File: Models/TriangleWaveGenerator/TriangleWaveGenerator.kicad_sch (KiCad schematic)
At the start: 2 parts, among them U1 LF412CP, U2 LM311N/NOPB

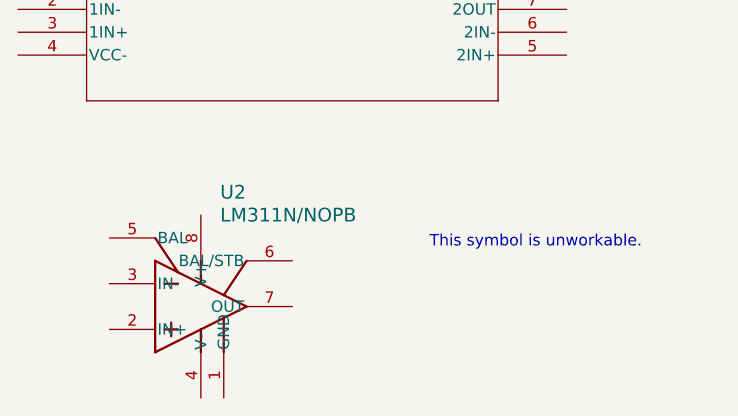
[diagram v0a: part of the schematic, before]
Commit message: Made custom symbol, much cleaner
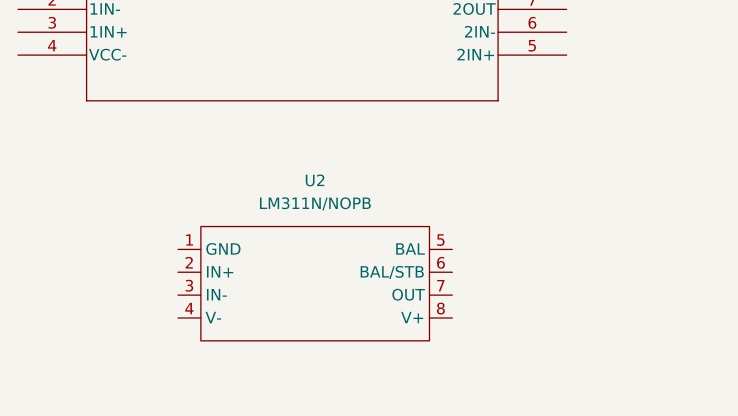
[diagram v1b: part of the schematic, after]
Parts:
- removed U2: LM311N/NOPB, N08E, symbol LM311:LM311N_NOPB
- added U2: LM311N/NOPB, symbol Custom:LM311N/NOPB
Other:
- note removed: "This symbol is unworkable."
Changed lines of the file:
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@@
 	(generator_version "9.0")
 	(paper "A4")
-	(text "This symbol is unworkable."
-		(exclude_from_sim no)
-		(at 139.7 108.966 0)
-		(effects
-			(font
-				(size 1.27 1.27)
-			)
-			(justify left top)
-		)
-	)
 	(symbol
-		(lib_id "LM311:LM311N_NOPB")
-		(at 109.22 111.76 0)
+		(lib_id "Custom:LM311N/NOPB")
+		(at 127 114.3 0)
 		(unit 1)
 		(exclude_from_sim no)
@@
 		(fields_autoplaced yes)
 		(property "Reference" "U2"
-			(at 116.4433 104.14 0)
+			(at 127 102.87 0)
 			(effects
 				(font
-					(size 1.524 1.524)
+					(size 1.27 1.27)
 				)
-				(justify left)
 			)
 		)
 		(property "Value" "LM311N/NOPB"
-			(at 116.4433 106.68 0)
-			(effects
-				(font
-					(size 1.524 1.524)
-				)
-				(justify left)
-			)
-		)
-		(property "Footprint" "N08E"
-			(at 109.22 111.76 0)
+			(at 127 105.41 0)
 			(effects
 				(font
 					(size 1.27 1.27)
-					(italic yes)
 				)
-				(hide yes)
 			)
 		)
-		(property "Datasheet" "https://www.ti.com/lit/gpn/lm311-n"
-			(at 109.22 111.76 0)
-			(effects
-				(font
-					(size 1.27 1.27)
-					(italic yes)
-				)
-				(hide yes)
-			)
-		)
-		(property "Description" ""
-			(at 109.22 111.76 0)
+		(property "Footprint" ""
+			(at 127 114.3 0)
 			(effects
 				(font
@@
 			)
 		)
+		(property "Datasheet" ""
+			(at 127 114.3 0)
+			(effects
+				(font
+					(size 1.27 1.27)
+				)
+				(hide yes)
+			)
+		)
+		(property "Description" ""
+			(at 127 114.3 0)
+			(effects
+				(font
+					(size 1.27 1.27)
+				)
+				(hide yes)
+			)
+		)
+		(pin "1"
+		)
 		(pin "2"
 		)
-		(pin "8"
+		(pin "3"
 		)
 		(pin "4"
 		)
-		(pin "1"
+		(pin "5"
 		)
 		(pin "6"
@@
 		(pin "7"
 		)
-		(pin "5"
-		)
-		(pin "3"
+		(pin "8"
 		)
 		(instances

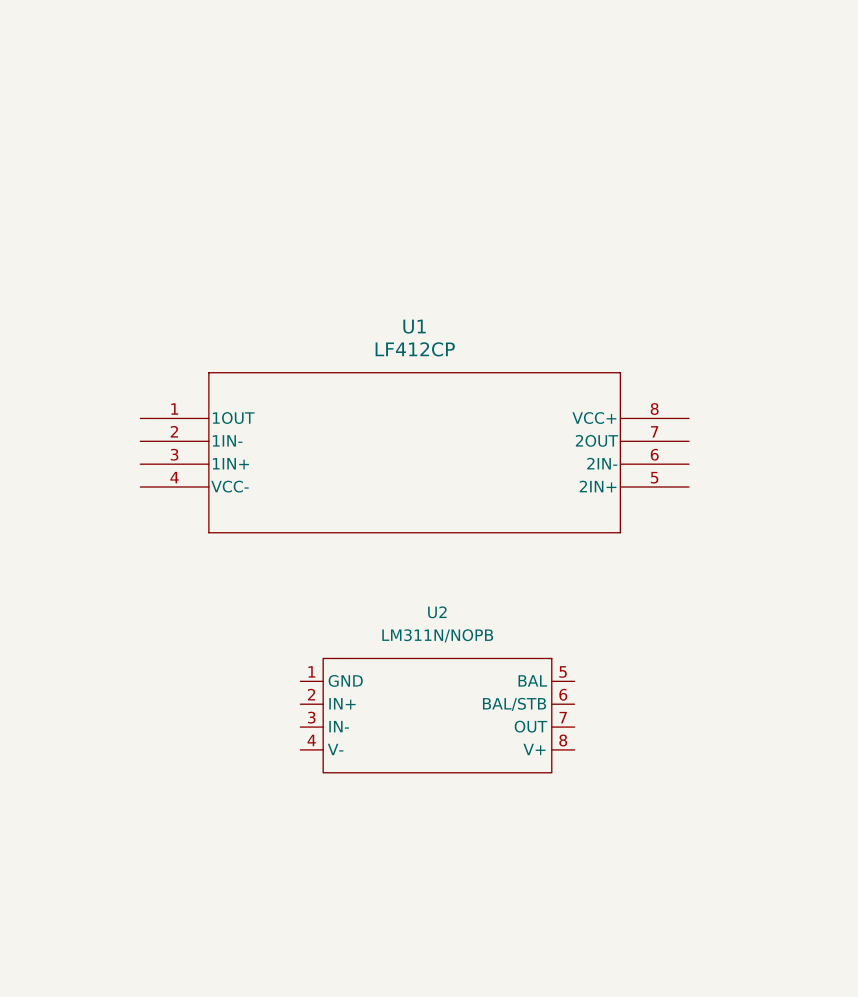
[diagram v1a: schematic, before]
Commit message: Need to migrate this to a hierarchical sheet
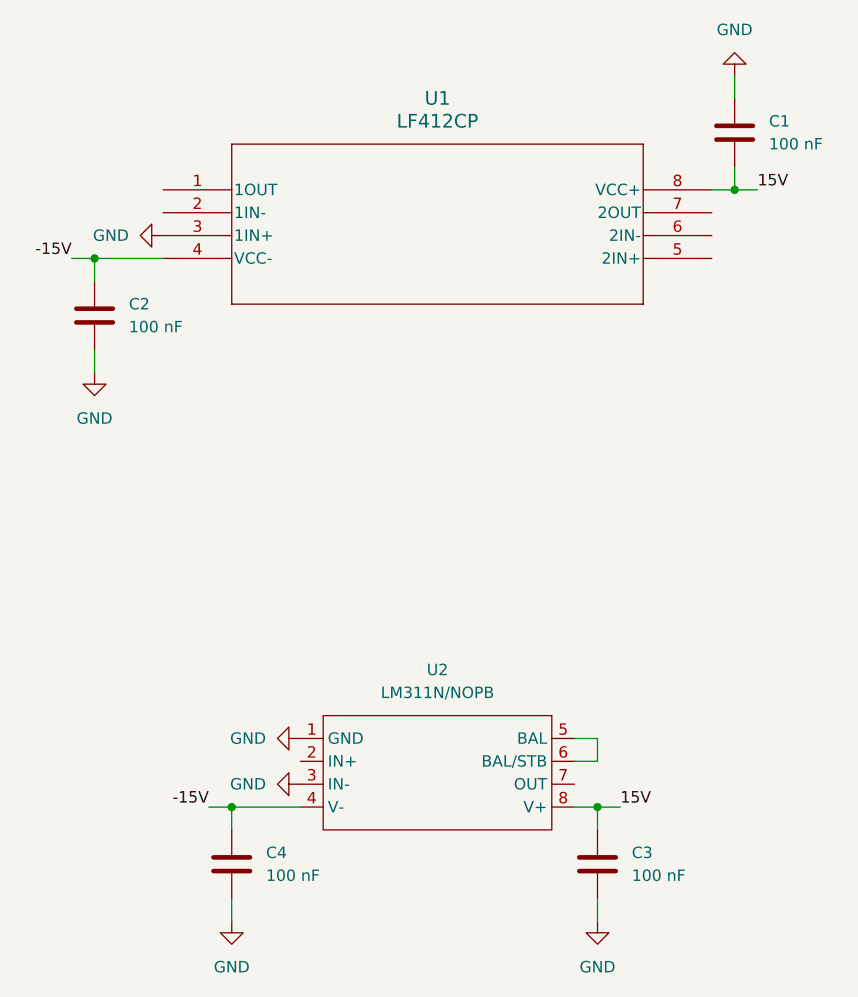
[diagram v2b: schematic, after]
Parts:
- added C1, C2, C3, C4: 100 nF, symbol Device:C
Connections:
- net GND: now reaches U2.1 (GND)
- net GND: now also U1.3 (1IN+), U2.3 (IN-), C1.1, C2.2, C3.2, C4.2
- net -15V: now reaches U2.4 (V-)
- net -15V: now also U1.4 (VCC-), C2.1, C4.1
- net at U2.5 (BAL): now also U2.6 (BAL/STB)
- net 15V: now reaches U2.8 (V+)
- net 15V: now also U1.8 (VCC+), C1.2, C3.1
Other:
- moved on the sheet: U1, U2

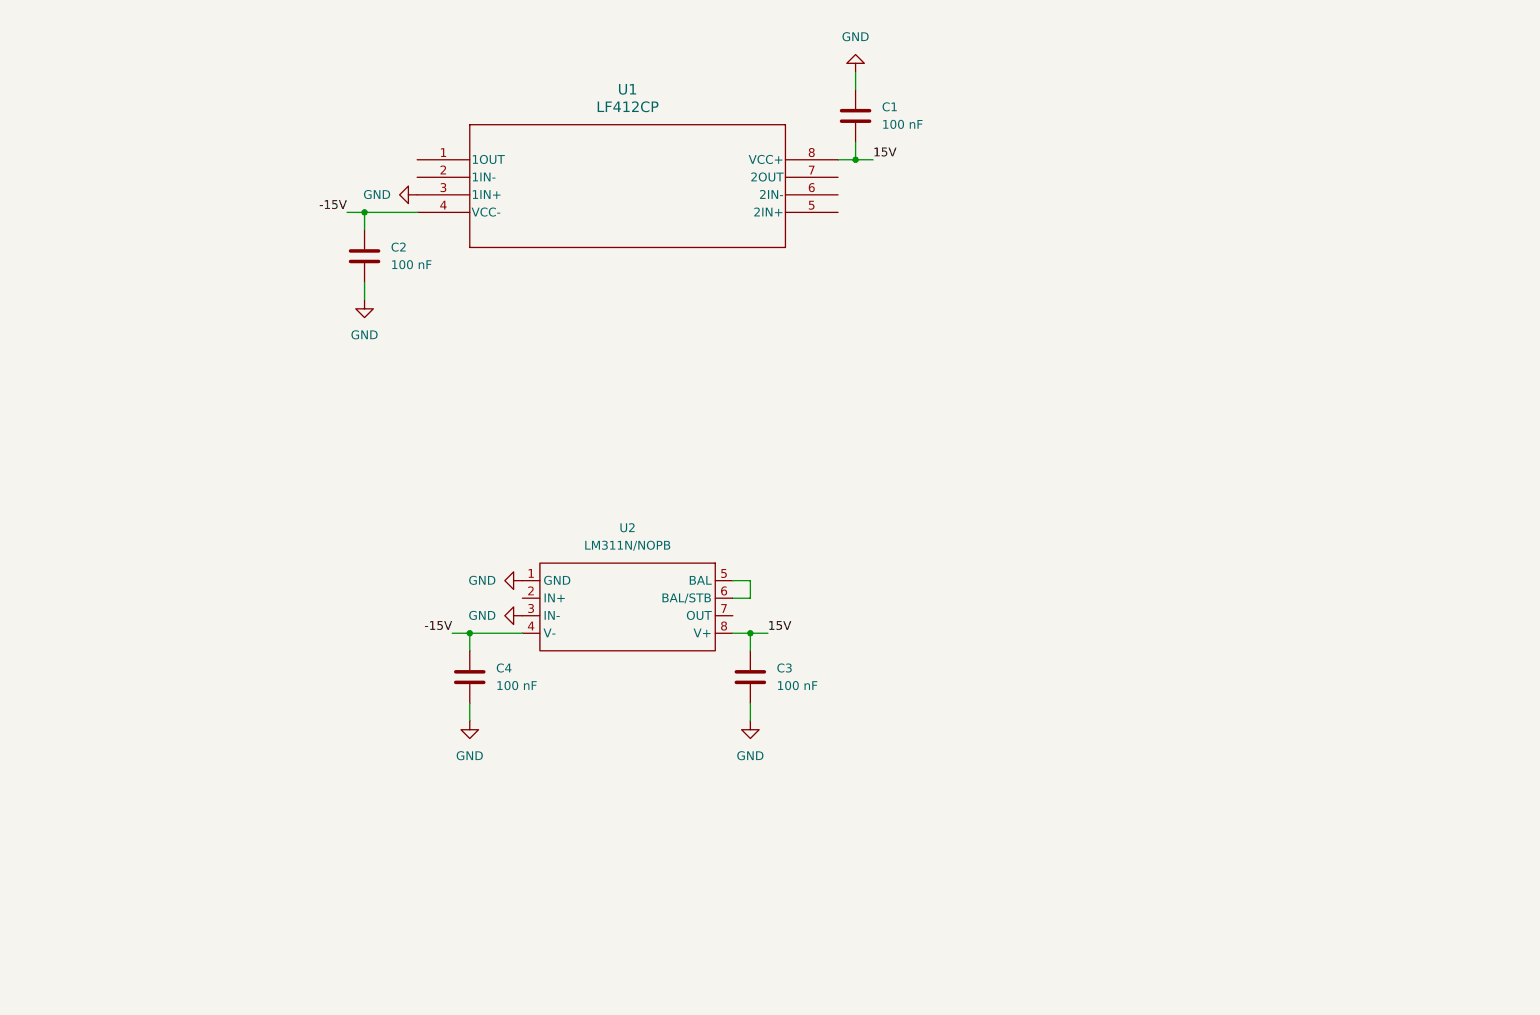
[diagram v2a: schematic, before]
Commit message: Sorting into hierarchical sheets
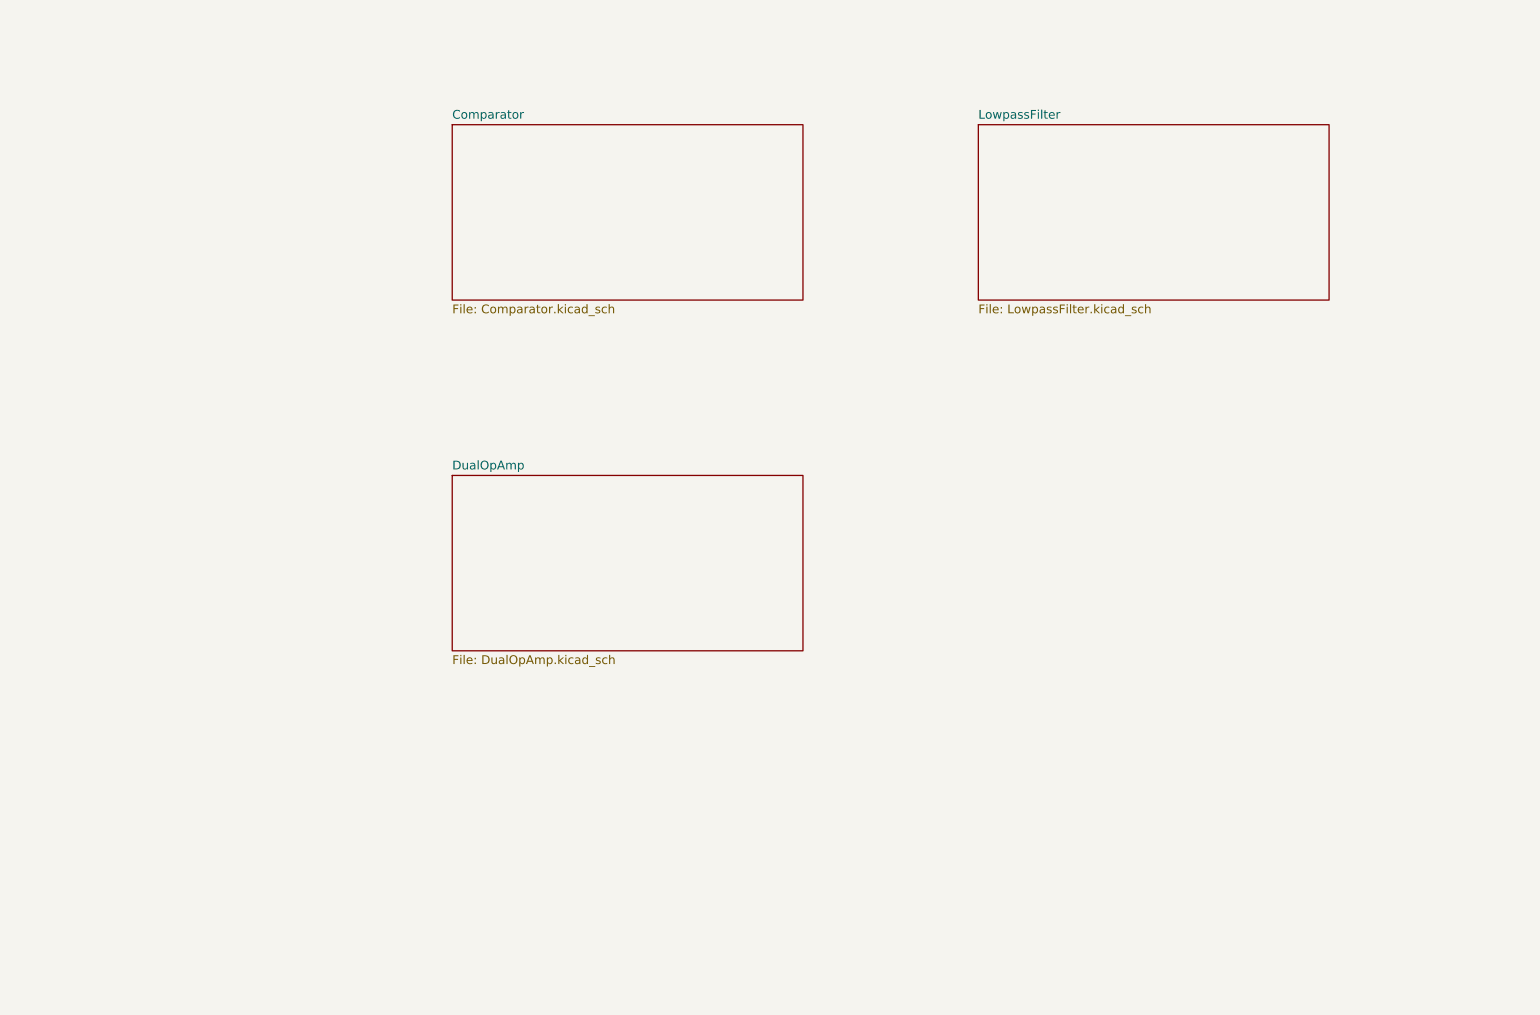
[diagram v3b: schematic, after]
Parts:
- removed C1, C2, C3, C4: 100 nF, symbol Device:C
- removed U1: LF412CP, P8, symbol LF412:LF412CP
- removed U2: LM311N/NOPB, symbol Custom:LM311N/NOPB
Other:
- added sheet Comparator (Comparator.kicad_sch)
- added sheet DualOpAmp (DualOpAmp.kicad_sch)
- added sheet LowpassFilter (LowpassFilter.kicad_sch)

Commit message: Filled in breadboard schematic, now need purchase links
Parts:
- added C6: 10 nF, symbol Device:C
- added R2: 4.7k, symbol Device:R_US
- added R3: 18k, symbol Device:R_US
- added R4: 100k, symbol Device:R_US
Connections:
- new net Comparator/Input(+): R2.1, R3.1
- new net Comparator/Output: R3.2, R4.1
- new net DualOpAmp/Input1(-): C6.1, R4.2
- new net DualOpAmp/Output1: C6.2
- new net DualOpAmp/Output2: R2.2
- no-connect marks 0 -> 2
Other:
- sheet Comparator ports: added -15V, 15V, Input(+), Output; removed none
- sheet DualOpAmp ports: added -15V, 15V, Input1(-), Output1, Output2; removed none
- sheet LowpassFilter ports: added Input, Output; removed none
- note added: "power supply: 15V and -15V regulated voltages, GND from Phase 0.1 main board power is buffered at IC pins with local decoupling capacitors on the breadboard"
- note added: "rectify and filter ~34 Hz lowpass connect either triangle wave or square wave output to check for circuit responsiveness without oscilloscope"
- note added: "square wave output ±15 V 0.96 kHz"
- note added: "triangle wave output ±3.92 V (with ±15 V supply) 0.96 kHz (15.0 V/ms)"

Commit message: Did the BOM
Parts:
- C6, R2, R3, R4: footprint (none) -> TwoTerminal:THT_10.16mm; now left out of the parts list
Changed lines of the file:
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@@
 		(unit 1)
 		(exclude_from_sim no)
-		(in_bom yes)
+		(in_bom no)
 		(on_board yes)
 		(dnp no)
@@
 			)
 		)
-		(property "Footprint" ""
+		(property "Footprint" "TwoTerminal:THT_10.16mm"
 			(at 57.404 67.564 90)
 			(effects
@@
 		)
 		(property "Description" "Resistor, US symbol"
+			(at 57.15 68.58 0)
+			(effects
+				(font
+					(size 1.27 1.27)
+				)
+				(hide yes)
+			)
+		)
+		(property "Purchase Link" ""
 			(at 57.15 68.58 0)
 			(effects
@@
 		(unit 1)
 		(exclude_from_sim no)
-		(in_bom yes)
+		(in_bom no)
 		(on_board yes)
 		(dnp no)
@@
 			)
 		)
-		(property "Footprint" ""
+		(property "Footprint" "TwoTerminal:THT_10.16mm"
 			(at 80.264 166.624 90)
 			(effects
@@
 		)
 		(property "Description" "Resistor, US symbol"
+			(at 80.01 167.64 0)
+			(effects
+				(font
+					(size 1.27 1.27)
+				)
+				(hide yes)
+			)
+		)
+		(property "Purchase Link" ""
 			(at 80.01 167.64 0)
 			(effects
@@
 		(unit 1)
 		(exclude_from_sim no)
-		(in_bom yes)
+		(in_bom no)
 		(on_board yes)
 		(dnp no)
@@
 			)
 		)
-		(property "Footprint" ""
+		(property "Footprint" "TwoTerminal:THT_10.16mm"
 			(at 65.024 117.856 90)
 			(effects
@@
 		)
 		(property "Description" "Resistor, US symbol"
+			(at 66.04 118.11 0)
+			(effects
+				(font
+					(size 1.27 1.27)
+				)
+				(hide yes)
+			)
+		)
+		(property "Purchase Link" ""
 			(at 66.04 118.11 0)
 			(effects
@@
 		(unit 1)
 		(exclude_from_sim no)
-		(in_bom yes)
+		(in_bom no)
 		(on_board yes)
 		(dnp no)
@@
 			)
 		)
-		(property "Footprint" ""
+		(property "Footprint" "TwoTerminal:THT_10.16mm"
 			(at 83.82 47.2948 0)
 			(effects
@@
 			(at 80.01 48.26 0)
 			(effects
+				(font
+					(size 1.27 1.27)
+				)
+				(hide yes)
+			)
+		)
+		(property "Purchase Link" ""
+			(at 80.01 48.26 0)
+			(effects

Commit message: Return to this later
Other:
- note added: "square wave output +11.9 V and -15.0 V TBD Hz"
- note added: "triangle wave output ±3.92 V (with ±15 V supply) 0.96 kHz (15.0 V/ms) rising edge: falling edge:"
- note removed: "square wave output ±15 V 0.96 kHz"
- note removed: "triangle wave output ±3.92 V (with ±15 V supply) 0.96 kHz (15.0 V/ms)"
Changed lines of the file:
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@@
 		)
 	)
-	(text "triangle wave output\n±3.92 V (with ±15 V supply)\n0.96 kHz (15.0 V/ms)"
+	(text "triangle wave output\n±3.92 V (with ±15 V supply)\n0.96 kHz (15.0 V/ms)\n\nrising edge:\n\n\nfalling edge:"
 		(exclude_from_sim no)
-		(at 99.06 35.56 0)
+		(at 137.922 48.768 0)
 		(effects
 			(font
@@
 		)
 	)
-	(text "square wave output\n±15 V\n0.96 kHz"
+	(text "square wave output\n+11.9 V and -15.0 V\nTBD Hz"
 		(exclude_from_sim no)
 		(at 137.16 132.08 0)

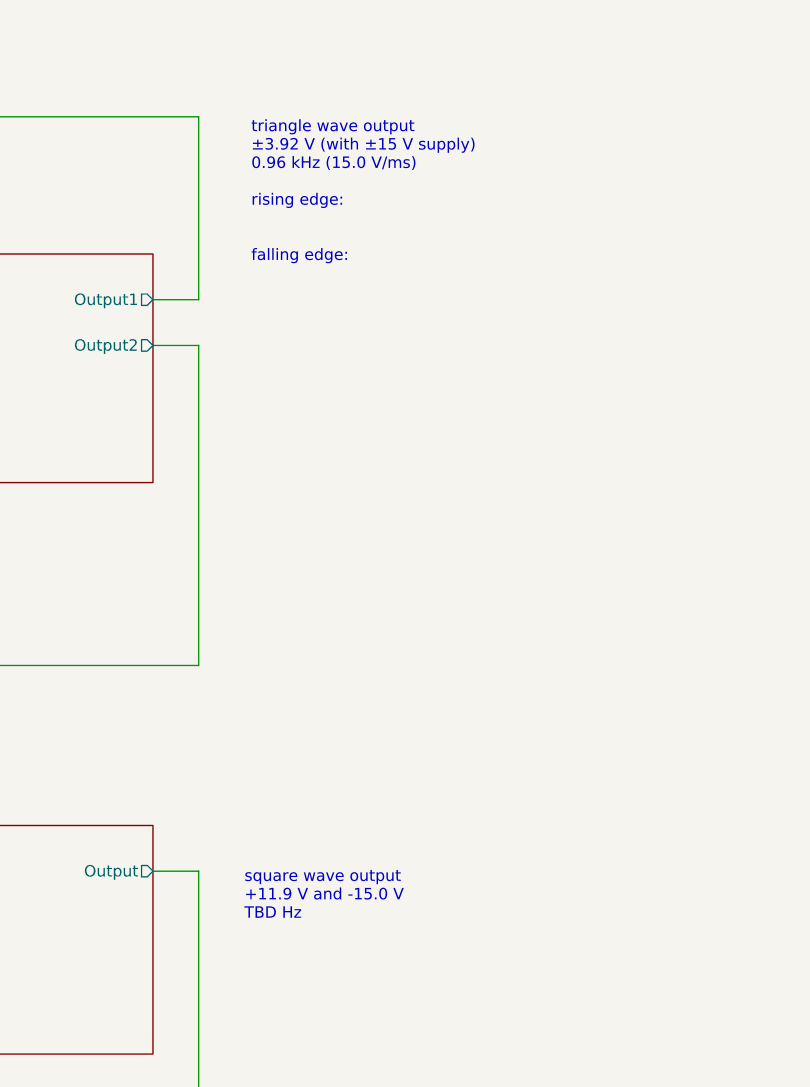
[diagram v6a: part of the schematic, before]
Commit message: Fixed the annotation
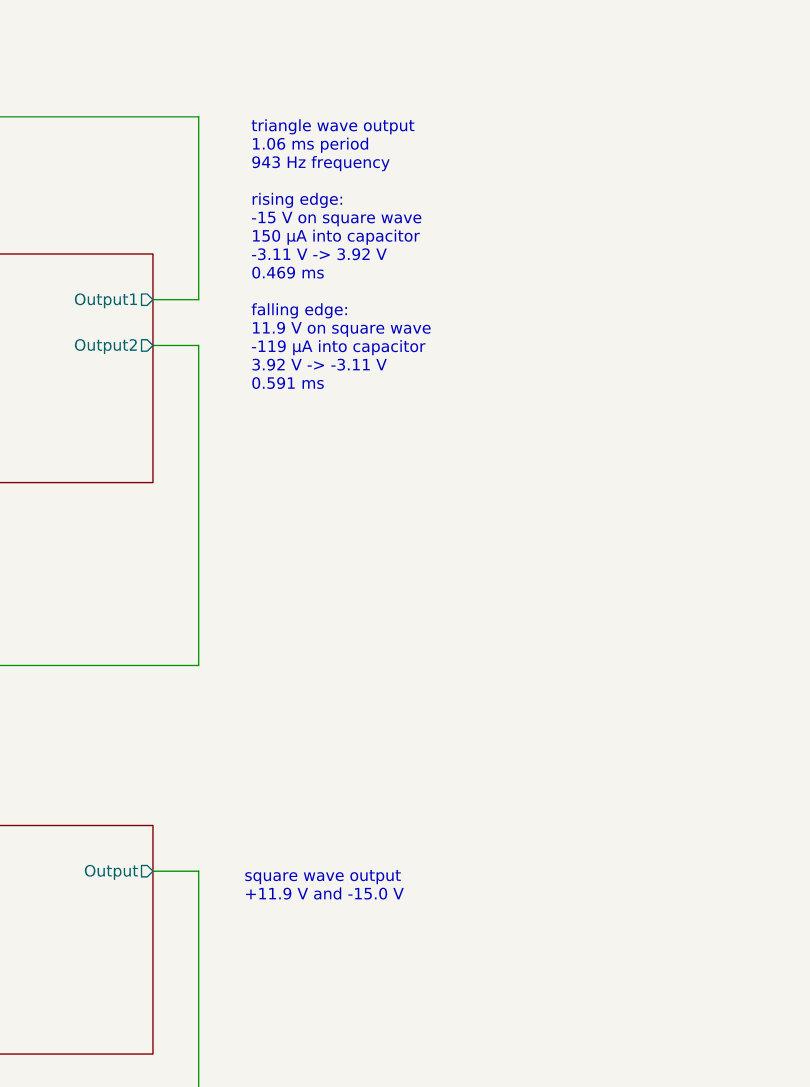
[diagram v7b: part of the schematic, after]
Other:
- note added: "square wave output +11.9 V and -15.0 V"
- note added: "triangle wave output 1.06 ms period 943 Hz frequency rising edge: -15 V on square wave 150 μA into capacitor -3.11 V -> 3.92 V 0.469 ms falling edge: 11.9 V on square wave -119 μA into capacitor 3.92 V -> -3.11 V 0.591 ms"
- note removed: "square wave output +11.9 V and -15.0 V TBD Hz"
- note removed: "triangle wave output ±3.92 V (with ±15 V supply) 0.96 kHz (15.0 V/ms) rising edge: falling edge:"
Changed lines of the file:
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@@
 		)
 	)
-	(text "triangle wave output\n±3.92 V (with ±15 V supply)\n0.96 kHz (15.0 V/ms)\n\nrising edge:\n\n\nfalling edge:"
+	(text "triangle wave output\n1.06 ms period\n943 Hz frequency\n\nrising edge:\n-15 V on square wave\n150 μA into capacitor\n-3.11 V -> 3.92 V\n0.469 ms\n\nfalling edge:\n11.9 V on square wave\n-119 μA into capacitor\n3.92 V -> -3.11 V\n0.591 ms"
 		(exclude_from_sim no)
 		(at 137.922 48.768 0)
@@
 		)
 	)
-	(text "square wave output\n+11.9 V and -15.0 V\nTBD Hz"
+	(text "square wave output\n+11.9 V and -15.0 V"
 		(exclude_from_sim no)
 		(at 137.16 132.08 0)
